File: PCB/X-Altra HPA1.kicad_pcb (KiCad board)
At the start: 2 copper layers, 130 x 150 mm, 160 parts, among them J1 L_In, J2 L_In, J3 HPOut, J4 AC_In, K1 C93402, Q1 BC850C, Q10 AO3400A, Q11 BC850C, Q12 BC860C, Q2 MJE15032, Q3 MJE15033, Q4 BC850C, Q5 MJE15032, Q6 MJE15033, Q7 BC850C, Q8 BC860C, Q9 BC850C, U1 OPA1656, U2 OPA1656, U3 TL072

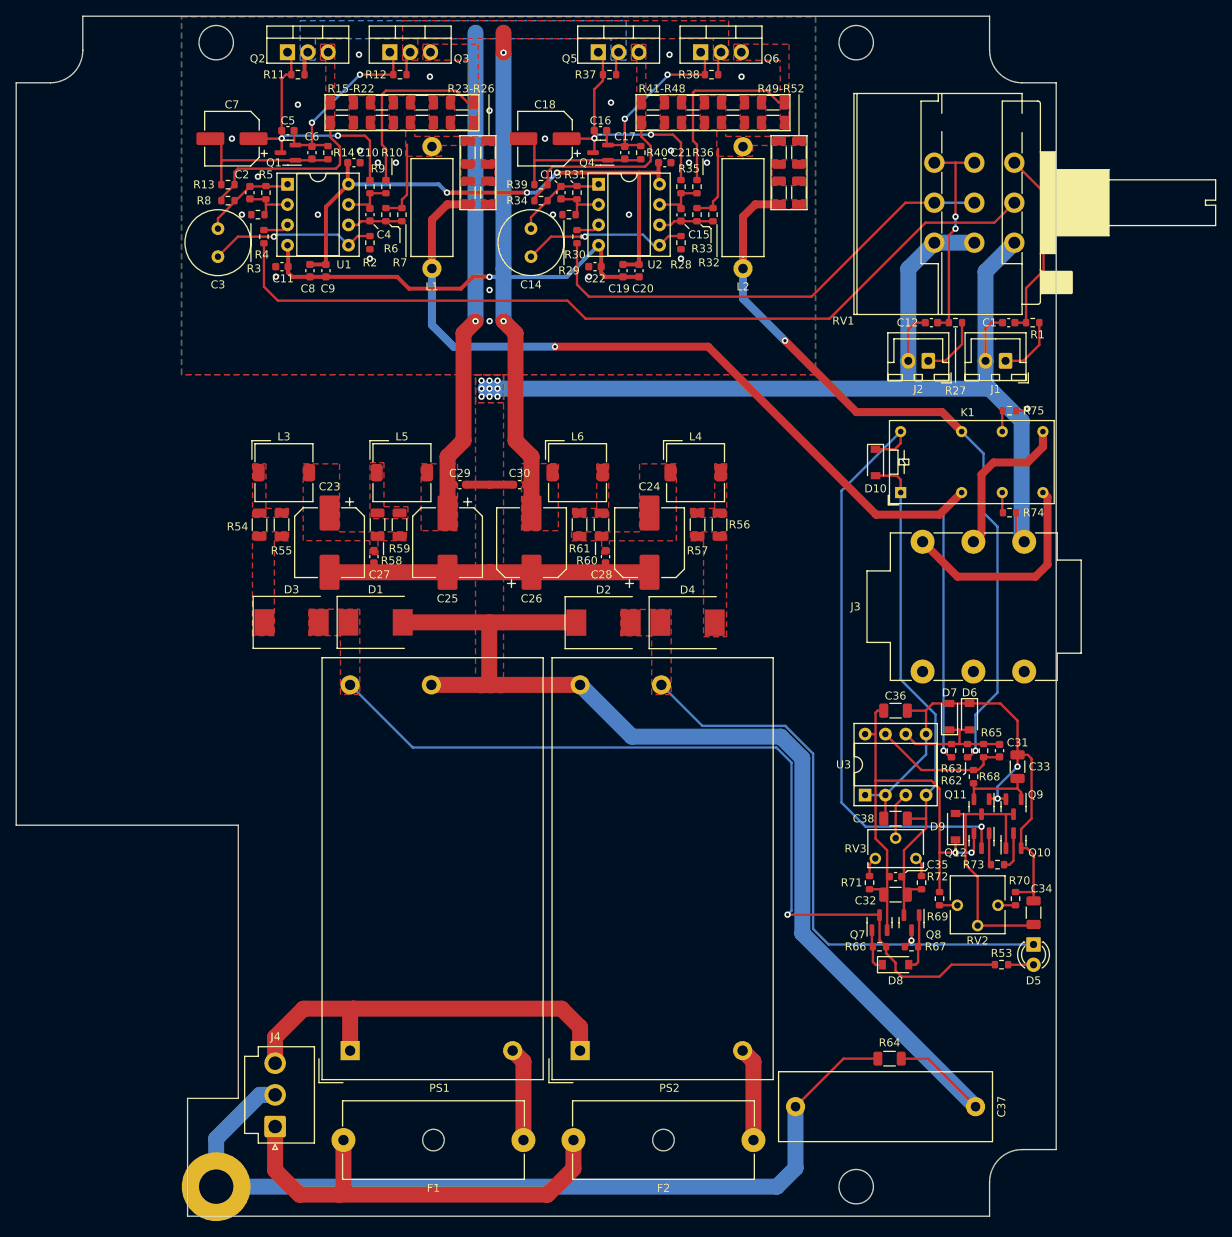
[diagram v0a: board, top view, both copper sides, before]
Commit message: Updated resistors to 1206 for less distortion
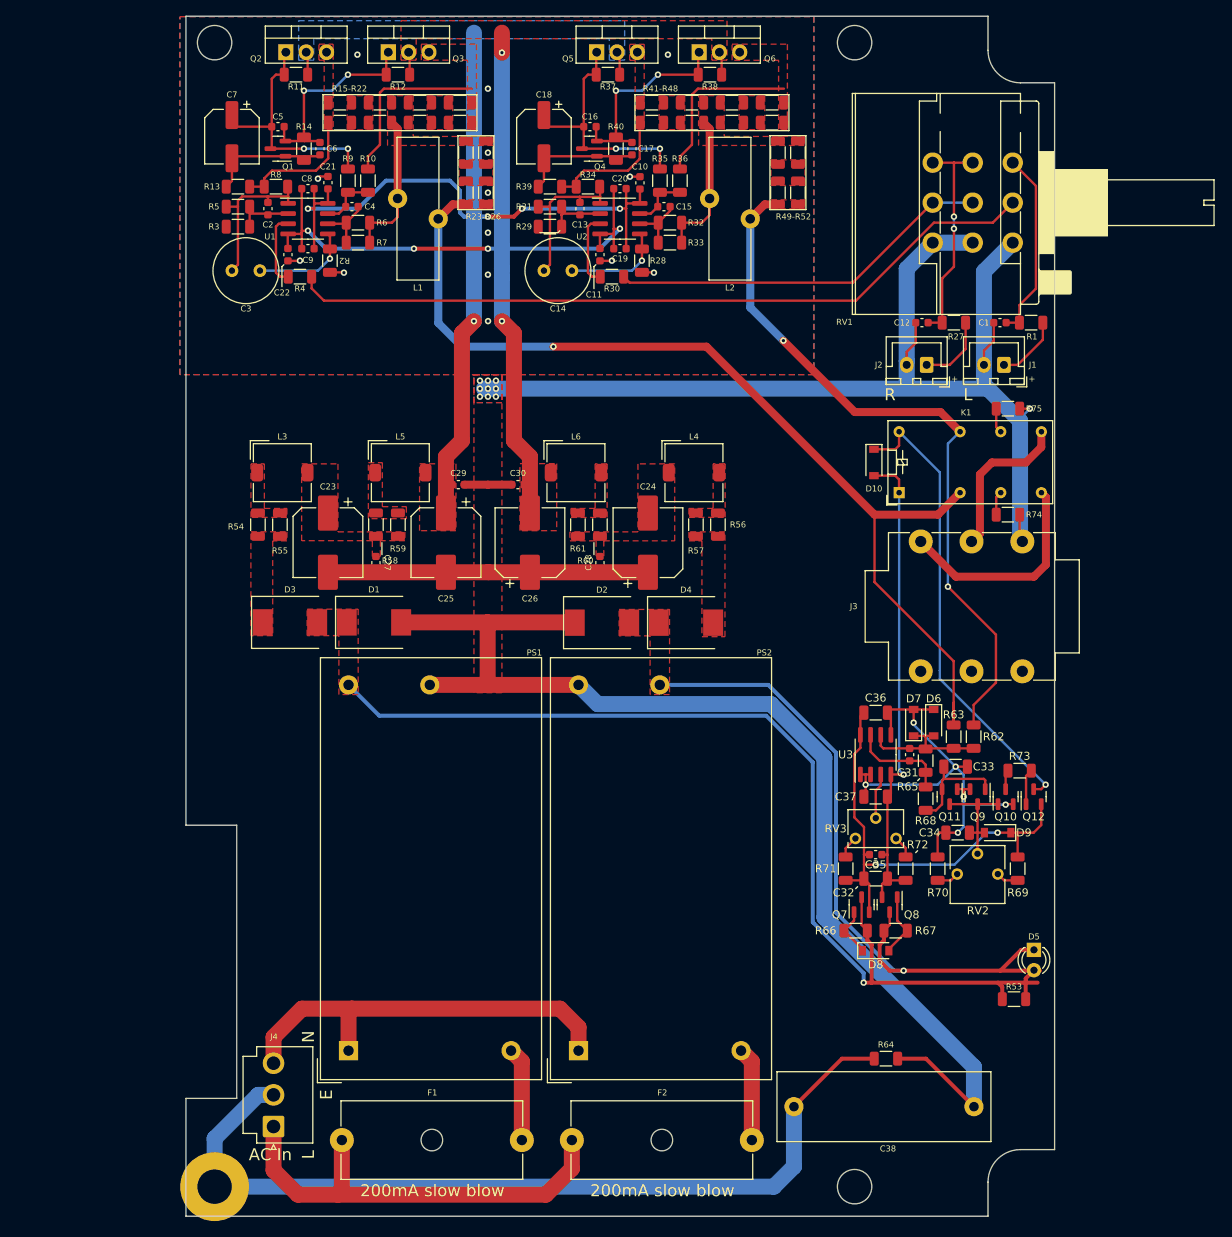
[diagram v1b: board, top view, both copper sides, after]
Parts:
- removed the C38 at (134.9, 108.8)
- added C37: 47u, Capacitor_SMD:C_1206_3216Metric, F.Cu at (132.5, 106.0)
- L1, L2: value 1u -> 0.8 - 1u 20 - 50mR; footprint Inductor_THT:L_Axial_L12.0mm_D5.0mm_P15.24mm_Horizontal_Fastron_MISC -> X-Altra HPA1:L_Toroid_D15mm_W4mm
- R1, R10, R11, R12, R13, R14, R2, R27, R28, R29, R3, R30, R31, R32, R33, R34, R35, R36, R37, R38, R39, R4, R40, R5, R53, R6, R62, R63, R65, R66, R67, R68, R69, R7, R70, R71, R72, R73, R74, R75, R8, R9: footprint Resistor_SMD:R_0603_1608Metric -> Resistor_SMD:R_1206_3216Metric
- U1, U2, U3: footprint Package_DIP:DIP-8_W7.62mm_Socket -> Package_SO:SOIC-8_3.9x4.9mm_P1.27mm
- moved C21 42.2 mm to (64.0, 29.2), turned to 90 degrees
- moved C11 39.8 mm to (98.0, 38.2), turned to 90 degrees
- moved C22 38.4 mm to (59.0, 38.2), turned to 90 degrees
- moved C10 35.8 mm to (103.0, 29.3), turned to 90 degrees
- moved C34 13.8 mm to (142.7, 110.5), turned to 180 degrees
- moved R73 12.1 mm to (150.5, 102.8), turned to 0 degrees
- moved C31 11.2 mm to (136.7, 100.8)
- moved C20 10.5 mm to (100.5, 30.0), turned to 180 degrees
- moved R69 10.5 mm to (150.2, 115.0)
- moved R70 10.4 mm to (140.2, 115.0)
- moved C8 10.3 mm to (61.5, 30.0), turned to 180 degrees
- moved Q12 8.52 mm to (152.2, 106.0), turned to 90 degrees
- moved L1 7.95 mm to (75.2, 32.5)
- moved L2 7.92 mm to (114.2, 32.5)
- moved C33 7.74 mm to (142.5, 102.2), turned to 0 degrees
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- renumbered C37 to C38
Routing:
- net Net-(C34-Pad1): track 32.8 -> 14.1 mm
- net Net-(D10-Pad1): track 75.8 -> 58.5 mm
- net VCC: track 111.0 -> 127.5 mm
- net VEE: track 75.7 -> 89.4 mm
- net Net-(L1-Pad1): track 10.2 -> 22.5 mm
- net GND1: track 69.5 -> 57.2 mm, vias 2 -> 6
- net Net-(R30-Pad1): track 60.3 -> 48.1 mm
- net Net-(L2-Pad1): track 9.68 -> 21.9 mm
- net Net-(R4-Pad1): track 106.9 -> 94.8 mm
- net -15V: track 121.6 -> 131.7 mm, vias 3 -> 6
- net Net-(C3-Pad2): track 21.2 -> 12.6 mm
- net Net-(C2-Pad2): track 11.4 -> 19.8 mm
- net Net-(C13-Pad2): track 11.2 -> 19.6 mm
- net Net-(C14-Pad2): track 20.9 -> 12.7 mm
- net GND: track 338.1 -> 346.1 mm, vias 36 -> 24
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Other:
- board size 130 x 150 mm -> 108.6 x 150 mm
- board text added: "+"
- board text added: "200mA slow blow"
- board text added: "AC In"
- board text added: "E"
- board text added: "L"
- board text added: "N"
- board text added: "R"

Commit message: Updated BOM
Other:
- board text added: "Anti pop timer adjust"
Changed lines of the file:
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@@
     (property "Sheetname" "")
     (attr through_hole)
-    (fp_text reference "RV2" (at -4.575 -2.495 180) (layer "F.SilkS")
+    (fp_text reference "RV2" (at -4.075 2.512791 180) (layer "F.SilkS")
       (effects (font (size 1 1) (thickness 0.15)))
     )
@@
     (property "Sheetname" "")
     (attr smd)
-    (fp_text reference "R2" (at 0 -1.82 180 unlocked) (layer "F.SilkS")
+    (fp_text reference "R2" (at 0 -1.82 unlocked) (layer "F.SilkS")
       (effects (font (size 0.75 0.75) (thickness 0.125)))
     )
@@
     (effects (font (size 0.75 0.75) (thickness 0.125)))
   )
+  (gr_text "Anti pop\ntimer\nadjust" (at 145.25 123.75) (layer "F.SilkS")
+    (effects (font (size 1.5 1.5) (thickness 0.2)))
+  )
   (gr_text "200mA slow blow" (at 77.050445 155.25) (layer "F.SilkS")

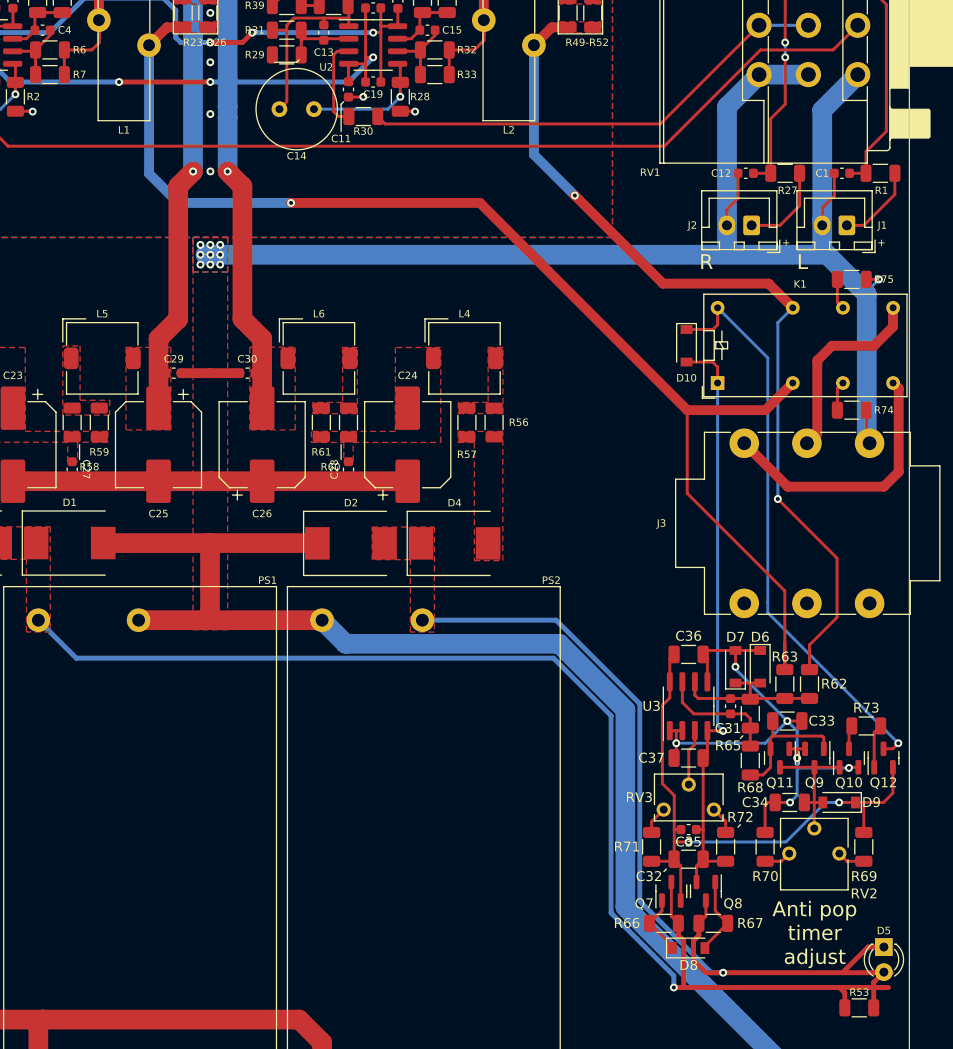
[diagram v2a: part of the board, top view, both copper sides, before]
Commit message: Fixed error with silkscreen and LED routing
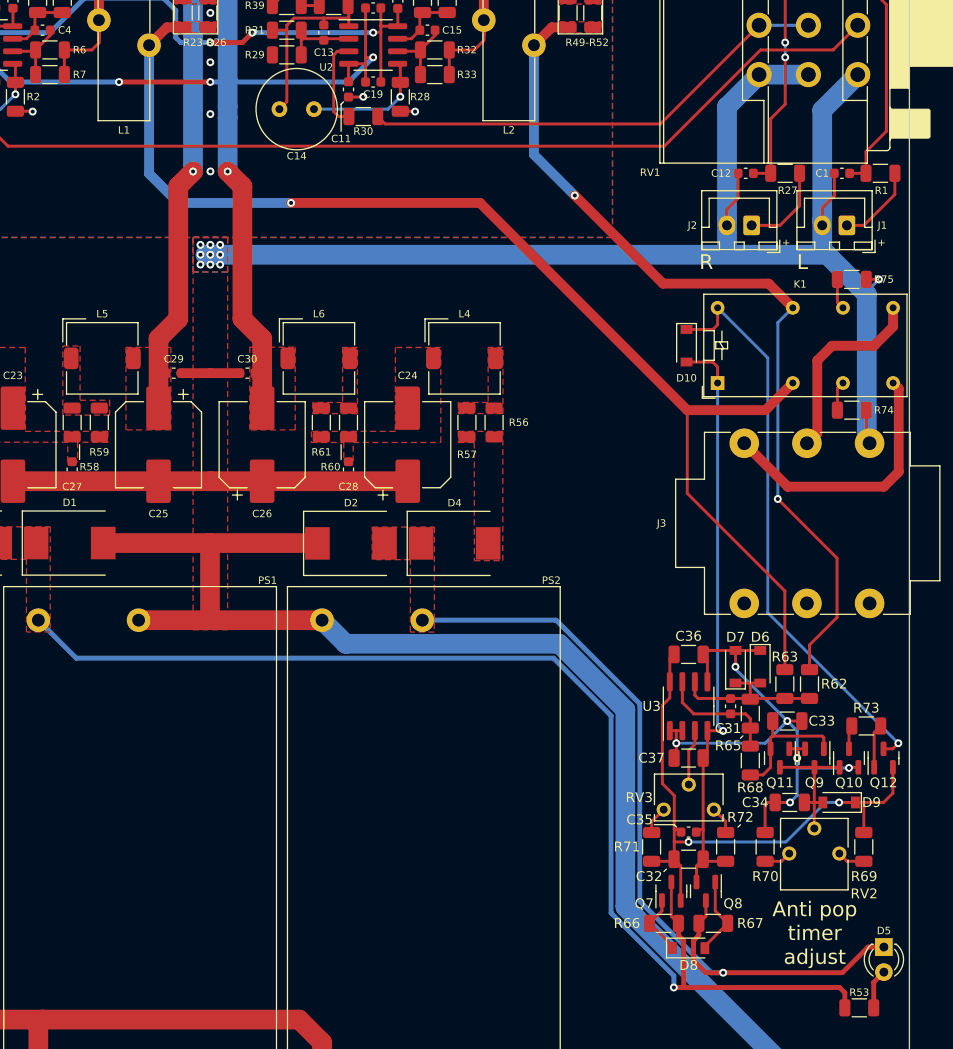
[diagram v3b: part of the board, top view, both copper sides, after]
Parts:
- L1, L2: value 0.8 - 1u 20 - 50mR -> 31 turns
- Q1, Q4: value BC850C -> BC847C
- R23, R24, R25, R26, R49, R50, R51, R52: value 3.3 -> 3
- R29, R3: value 2.2k -> 2.7k
- R30, R35, R4, R9: value 120 -> 121
- R54, R55, R56, R57, R58, R59, R60, R61: value 10 -> 4.99
- U3: value TL072 -> TL082
- moved C35 0.25 mm to (132.5, 113.5)
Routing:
- net VEE: track 89.4 -> 84.4 mm
- net VCC: track 127.5 -> 122.5 mm
- net L_Out: track 126.1 -> 123.9 mm
